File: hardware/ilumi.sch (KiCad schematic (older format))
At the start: 43 parts, among them J1 MICROUSB, P1 2PIN_MALE, U1 ESP-12E, U2 PCA9685, U3 AZ1117E

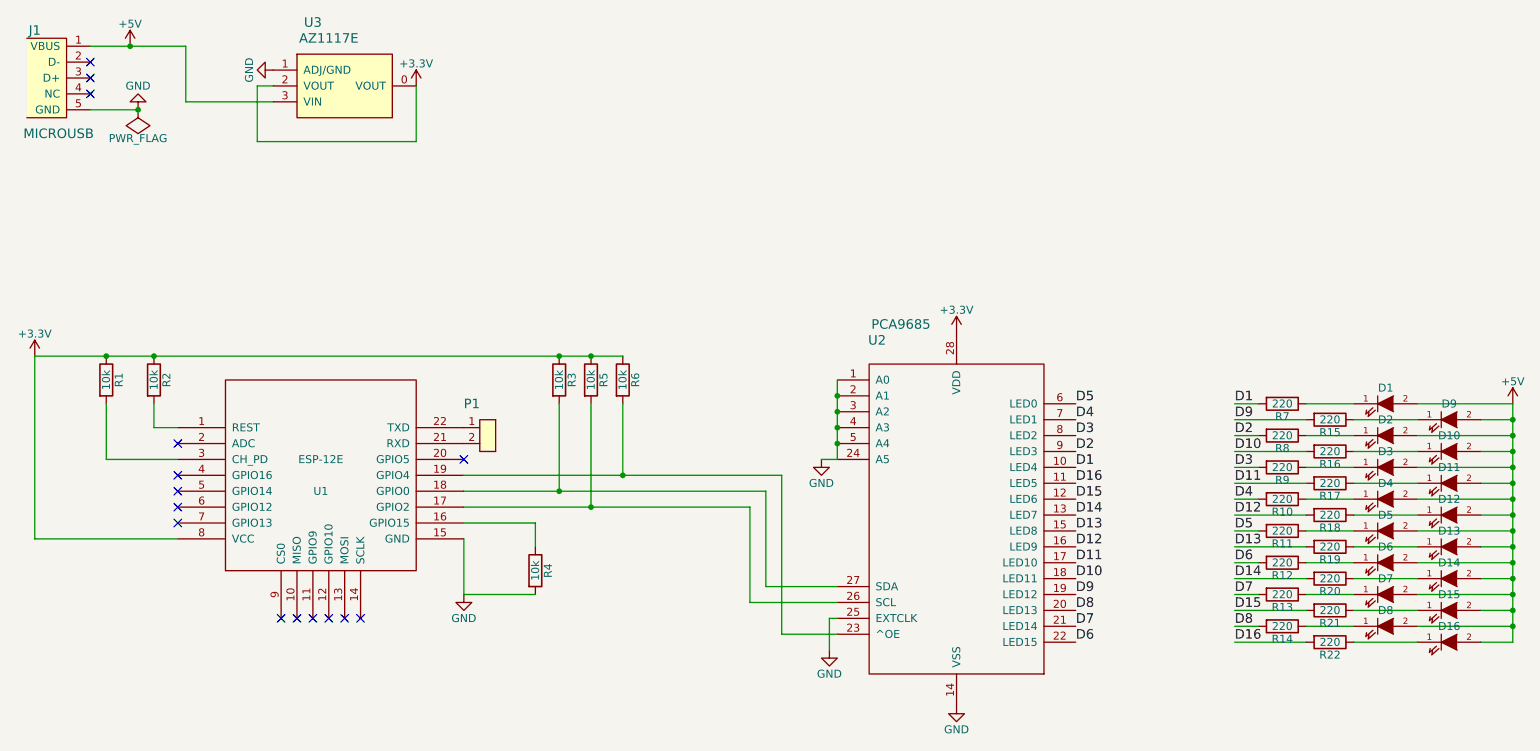
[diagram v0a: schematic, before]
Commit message: [PCB] Fix v1 issues - Add GND in UART header - Power LEDs driver with 5V
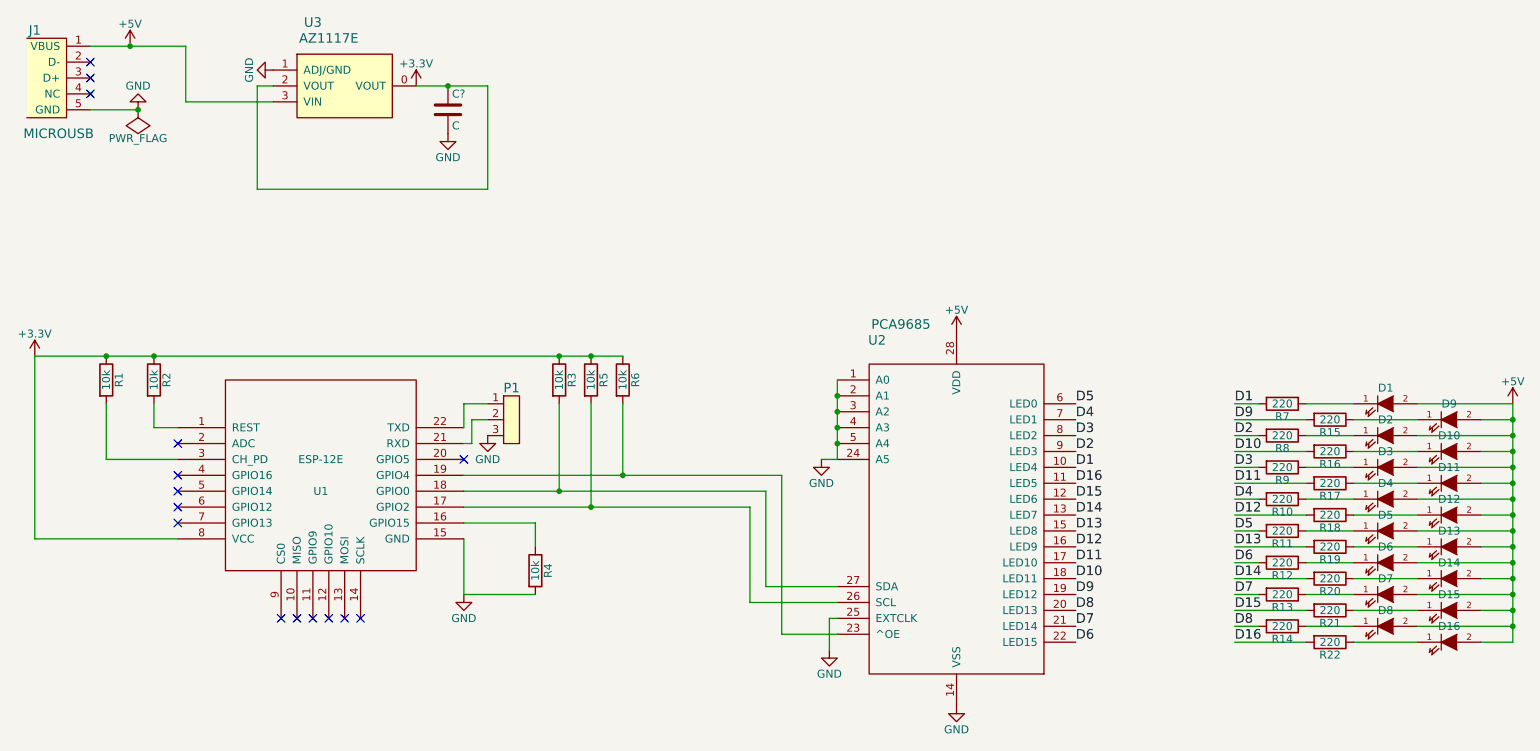
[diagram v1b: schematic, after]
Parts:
- removed P1: 2PIN_MALE, sip:SIP2, symbol 2PIN_MALE
- added C?: C, symbol C
- added P1: 3PIN_MALE, symbol 3PIN_MALE
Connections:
- net +3V3: now also C?.1; no longer U2.28 (VDD)
- net +5V: now also U2.28 (VDD)
- net GND: now also C?.2, P1.3
- net at U1.21 (RXD): now also P1.2
- net at U1.22 (TXD): now also P1.1
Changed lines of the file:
@@
 Connection ~ 6650 4100
-$Comp
-L +3.3V #PWR09
-U 1 1 57C58820
-P 7400 3400
-F 0 "#PWR09" H 7400 3250 50  0001 C CNN
-F 1 "+3.3V" H 7400 3540 50  0000 C CNN
-F 2 "" H 7400 3400 50  0000 C CNN
-F 3 "" H 7400 3400 50  0000 C CNN
-	1    7400 3400
-	1    0    0    -1
-$EndComp
 $Comp
 L R R7
@@
 	3100 1850 3000 1850
 Wire Wire Line
-	3000 1850 3000 2200
-Wire Wire Line
-	3000 2200 4000 2200
-Wire Wire Line
-	4000 2200 4000 1850
+	3000 1850 3000 2500
 $Comp
 L +3.3V #PWR011
@@
 F 3 "" H 4000 1850 50  0000 C CNN
 	1    4000 1850
-	1    0    0    -1
-$EndComp
-$Comp
-L 2PIN_MALE P1
-U 1 1 57C6C025
-P 4400 4050
-F 0 "P1" H 4350 4250 60  0000 C CNN
-F 1 "2PIN_MALE" H 4400 3850 60  0001 C CNN
-F 2 "sip:SIP2" H 4350 3850 60  0001 C CNN
-F 3 "" H 4350 3850 60  0001 C CNN
-	1    4400 4050
 	1    0    0    -1
 $EndComp
@@
 Connection ~ 2200 1600
 Connection ~ 2250 2000
+$Comp
+L +5V #PWR?
+U 1 1 59522E21
+P 7400 3400
+F 0 "#PWR?" H 7400 3250 50  0001 C CNN
+F 1 "+5V" H 7400 3540 50  0000 C CNN
+F 2 "" H 7400 3400 50  0000 C CNN
+F 3 "" H 7400 3400 50  0000 C CNN
+	1    7400 3400
+	1    0    0    -1
+$EndComp
+$Comp
+L 3PIN_MALE P1
+U 1 1 59523205
+P 4550 3950
+F 0 "P1" H 4600 4150 60  0000 C CNN
+F 1 "3PIN_MALE" H 4550 3750 60  0001 C CNN
+F 2 "" H 4600 3800 60  0001 C CNN
+F 3 "" H 4600 3800 60  0001 C CNN
+	1    4550 3950
+	1    0    0    -1
+$EndComp
+Wire Wire Line
+	4300 4000 4300 3850
+Wire Wire Line
+	4300 3850 4450 3850
+Wire Wire Line
+	4300 4100 4350 4100
+Wire Wire Line
+	4350 4100 4350 3950
+Wire Wire Line
+	4350 3950 4450 3950
+$Comp
+L GND #PWR?
+U 1 1 59523557
+P 4450 4050
+F 0 "#PWR?" H 4450 3800 50  0001 C CNN
+F 1 "GND" H 4450 3900 50  0000 C CNN
+F 2 "" H 4450 4050 50  0000 C CNN
+F 3 "" H 4450 4050 50  0000 C CNN
+	1    4450 4050
+	1    0    0    -1
+$EndComp
+$Comp
+L C C?
+U 1 1 59523C8A
+P 4200 2000
+F 0 "C?" H 4225 2100 50  0000 L CNN
+F 1 "C" H 4225 1900 50  0000 L CNN
+F 2 "" H 4238 1850 50  0000 C CNN
+F 3 "" H 4200 2000 50  0000 C CNN
+	1    4200 2000
+	1    0    0    -1
+$EndComp
+$Comp
+L GND #PWR?
+U 1 1 59523D3D
+P 4200 2150
+F 0 "#PWR?" H 4200 1900 50  0001 C CNN
+F 1 "GND" H 4200 2000 50  0000 C CNN
+F 2 "" H 4200 2150 50  0000 C CNN
+F 3 "" H 4200 2150 50  0000 C CNN
+	1    4200 2150
+	1    0    0    -1
+$EndComp
+Wire Wire Line
+	4000 1850 4450 1850
+Wire Wire Line
+	3000 2500 4450 2500
+Wire Wire Line
+	4450 2500 4450 1850
+Connection ~ 4200 1850
 $EndSCHEMATC
